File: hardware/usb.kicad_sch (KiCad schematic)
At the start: 46 parts, among them J2 USB_C_Receptacle_USB2.0, J3 BATTERY, Q1 Q_Dual_NMOS_G1S2G2D2S1D1, SW3 POWER, U7 TLV62569DBV, U8 MP2723, U9 MAX17048G

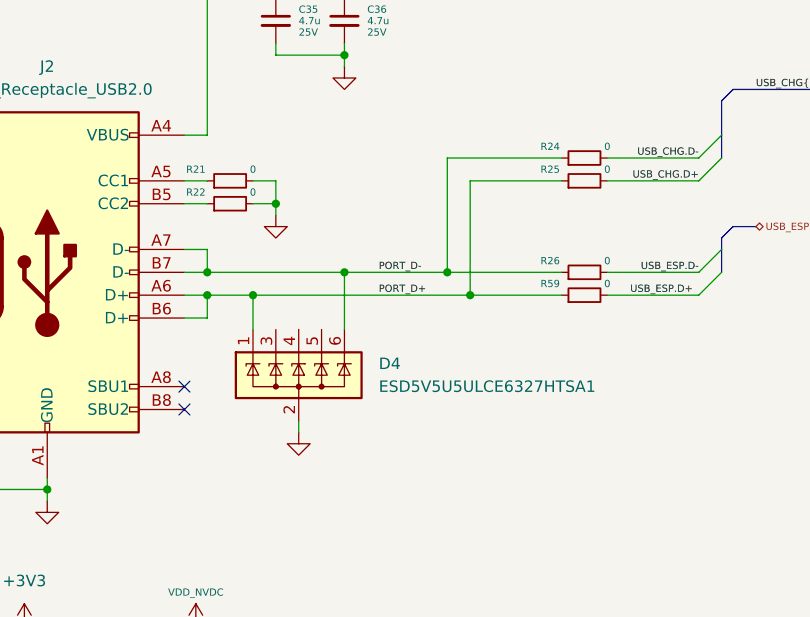
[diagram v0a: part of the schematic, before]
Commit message: merged in lcdboard test work
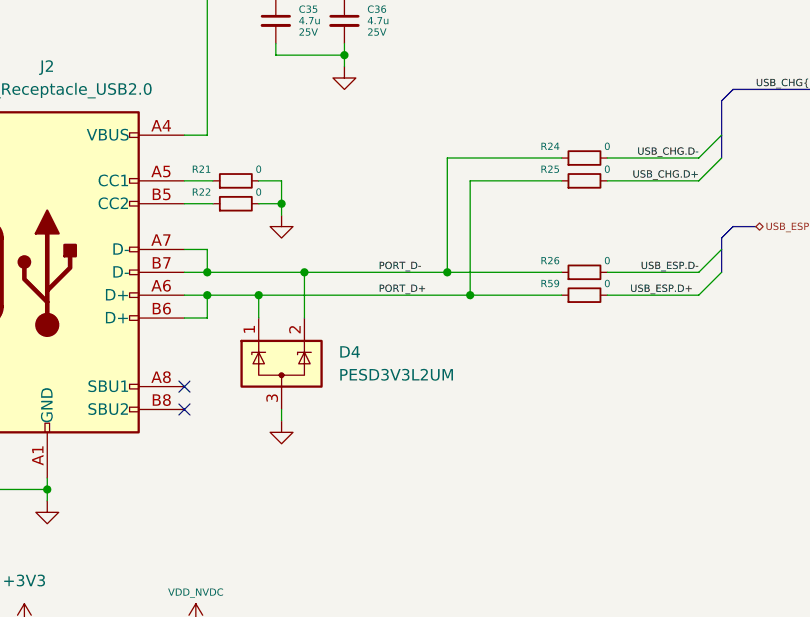
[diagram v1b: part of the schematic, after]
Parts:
- removed D4: ESD5V5U5ULCE6327HTSA1, Package_TO_SOT_SMD:SOT-363_SC-70-6, symbol Power_Protection:SP0505BAJT
- added D4: PESD3V3L2UM, Package_TO_SOT_SMD:SOT-883, symbol Power_Protection:SP0502BAHT
- Q1: footprint (none) -> Package_TO_SOT_SMD:SOT-363_SC-70-6
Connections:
- net GND: now also D4.3 (A)
- net PORT_D+: now also D4.1 (K)
- net PORT_D-: now also D4.2 (K)
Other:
- moved on the sheet: R21, R22
